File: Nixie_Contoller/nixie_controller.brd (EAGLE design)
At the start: 112.5 x 51.7 mm, 42 parts, among them IC1 DS1307, IC2 MAX1771ESA, IC3 7805T, J1 CON-SOCJ-2155, Q1 16MHz, T1 IRF644PBF, U1 328P, U2 HU2032-LF, X1 22-23-2021, Y2 32.768kHz

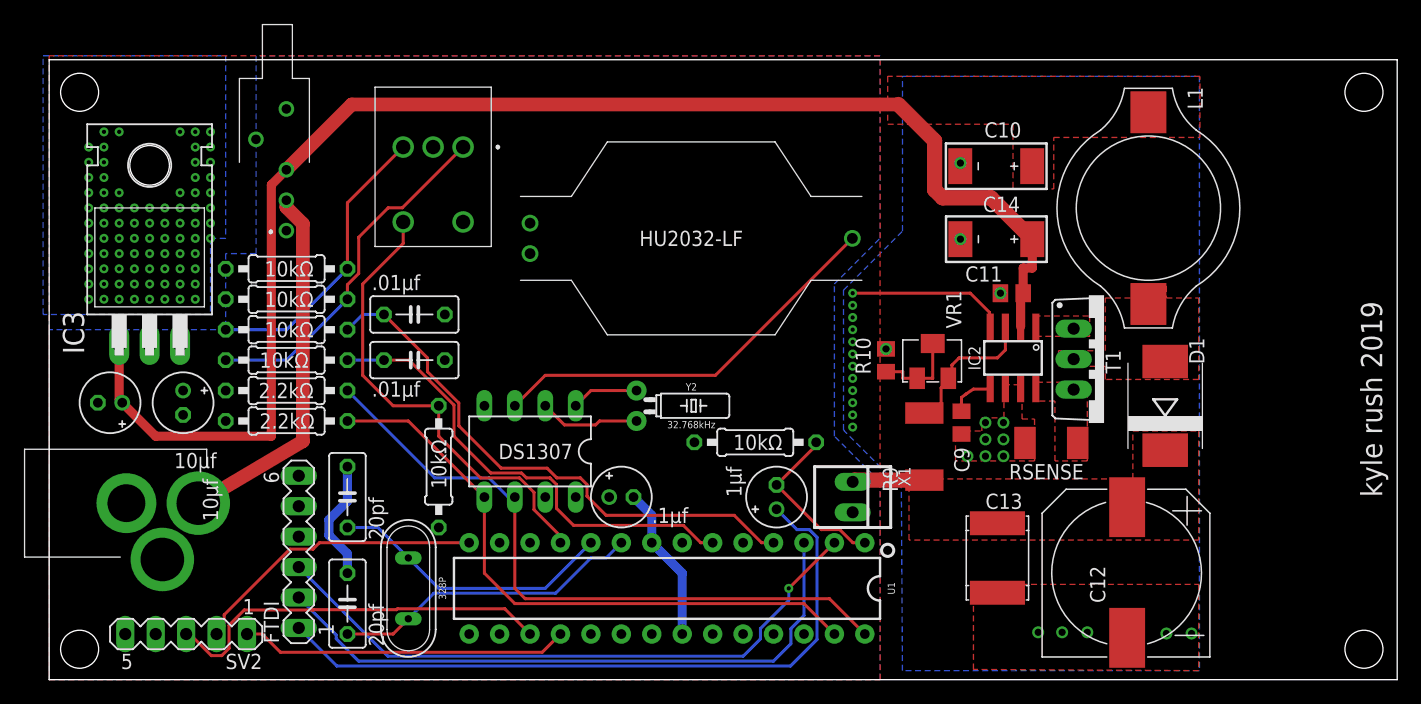
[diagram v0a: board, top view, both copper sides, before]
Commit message: Updates parts to Digikey equivalent, adds BOM, adds SHDN to pin 5
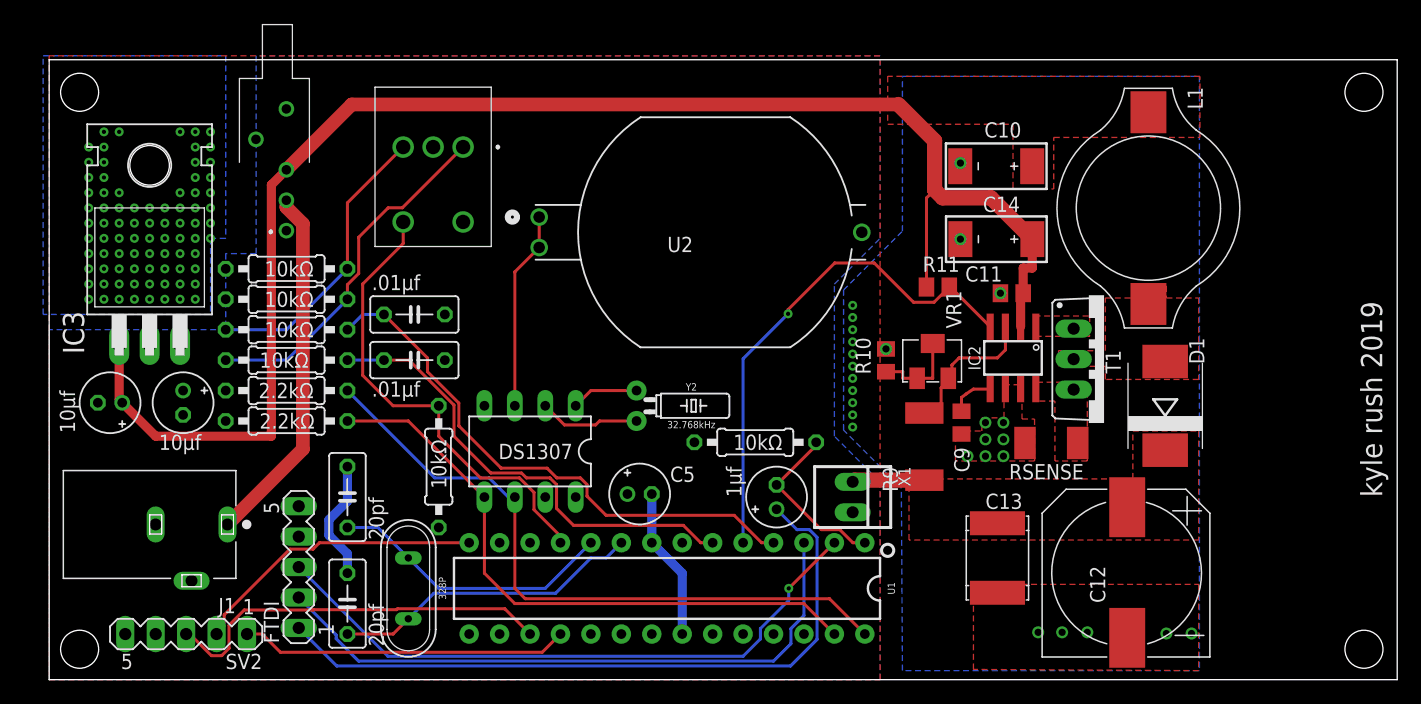
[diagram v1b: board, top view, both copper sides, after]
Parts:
- added R11: 10k, rcl:M0805
- C5: value .1μf -> .1uF
- FTDI: device con-lstb:MA06-1 -> con-lstb:MA05-1
- J1: value CON-SOCJ-2155 -> PJ-102A; device SamacSys_Parts:CONSOCJ2155 -> PJ-102A:CUI_PJ-102A
- U2: value HU2032-LF -> 120591-1; device SamacSys_Parts:HU2032LF -> TE Connectivity AMP Connectors 120591-1:CONN3_120591-1
- moved U2 14.2 mm to (54.4, 37.3)
- moved J1 4.44 mm to (8.38, 13.0), turned to 180 degrees
- moved C5 1.55 mm to (49.3, 15.5)
- moved FTDI 1.27 mm to (20.8, 9.40)
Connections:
- new net SHDN: IC2.4, R11.2, U1.5
- net +12V: now also R11.1
- net GND: now also FTDI.5; no longer FTDI.6, IC2.4, U2.1
- net N$1: now also U2.1
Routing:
- net SHDN: track 0.00 -> 42.7 mm, vias 0 -> 1
- net N$1: track 34.0 -> 16.6 mm
- net GND: track 36.6 -> 22.9 mm, vias 110 -> 109
- net +12V: track 121.1 -> 129.5 mm
- net N$6: track 30.8 -> 30.2 mm

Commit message: Production ready board with BOMS
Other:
- board text added: "kyle rush 2020"
- board text removed: "kyle rush 2019"
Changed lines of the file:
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@@
 <setting verticaltext="up"/>
 </settings>
-<grid distance="10" unitdist="mil" unit="mil" style="lines" multiple="1" display="no" altdistance="5" altunitdist="mil" altunit="mil"/>
+<grid distance="10" unitdist="mil" unit="mm" style="lines" multiple="1" display="no" altdistance="5" altunitdist="mil" altunit="mil"/>
 <layers>
 <layer number="1" name="Top" color="4" fill="1" visible="yes" active="yes"/>
@@
 <hole x="109.728" y="49.022" drill="3.175"/>
 <hole x="109.728" y="2.54" drill="3.175"/>
-<text x="111.252" y="15.24" size="1.778" layer="21" rot="R90">kyle rush 2019</text>
+<text x="111.252" y="15.24" size="1.778" layer="21" rot="R90">kyle rush 2020</text>
 <wire x1="-0.0254" y1="-63.5" x2="-0.0254" y2="-72.0852" width="0.2032" layer="47"/>
 <wire x1="-0.0254" y1="-72.0852" x2="-0.0254" y2="-73.66" width="0.2032" layer="47"/>
@@
 <element name="VR1" library="nick" package="BOURNS-3214W" value="5K" x="73.738" y="26.554" smashed="yes" rot="R270">
 <attribute name="NAME" x="74.858" y="32.472" size="1.27" layer="25" rot="R270"/>
-<attribute name="VALUE" x="74.36" y="31.146" size="1.27" layer="27" rot="R270"/>
 </element>
 <element name="C10" library="nick" package="C-EIA-7343" value="100uF,35V" x="79.038" y="42.854" smashed="yes" rot="R180">
@@
 </element>
 <element name="C11" library="rcl" package="C0805" value="100n" x="80.338" y="32.254" smashed="yes" rot="R180">
-<attribute name="NAME" x="76.449" y="33.224" size="1.27" layer="25"/>
+<attribute name="NAME" x="76.449" y="33.478" size="1.27" layer="25"/>
 <attribute name="VALUE" x="79.989" y="33.306" size="1.27" layer="27"/>
 </element>
@@
 <attribute name="POPULARITY" value="45" x="74.168" y="32.766" size="1.778" layer="27" display="off"/>
 <attribute name="SPICEPREFIX" value="R" x="74.168" y="32.766" size="1.778" layer="27" display="off"/>
-<attribute name="VALUE" x="72.898" y="30.226" size="1.27" layer="27"/>
 </element>
 <element name="FTDI" library="con-lstb" library_urn="urn:adsk.eagle:library:162" package="MA05-1" package3d_urn="urn:adsk.eagle:package:8332/1" value="" x="20.828" y="9.398" smashed="yes" rot="R90">

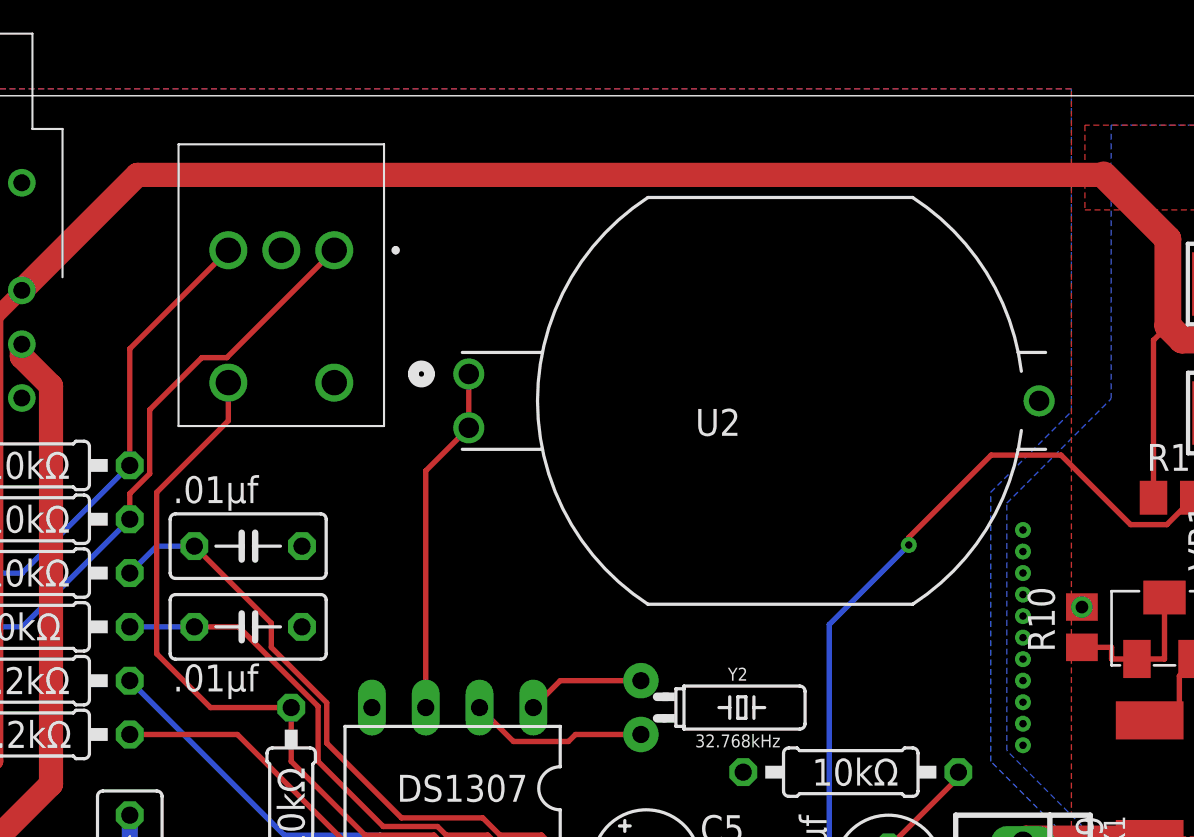
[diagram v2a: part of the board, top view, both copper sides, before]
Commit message: Reconfigures controller, configures clock to pull sketch down SHDN pin
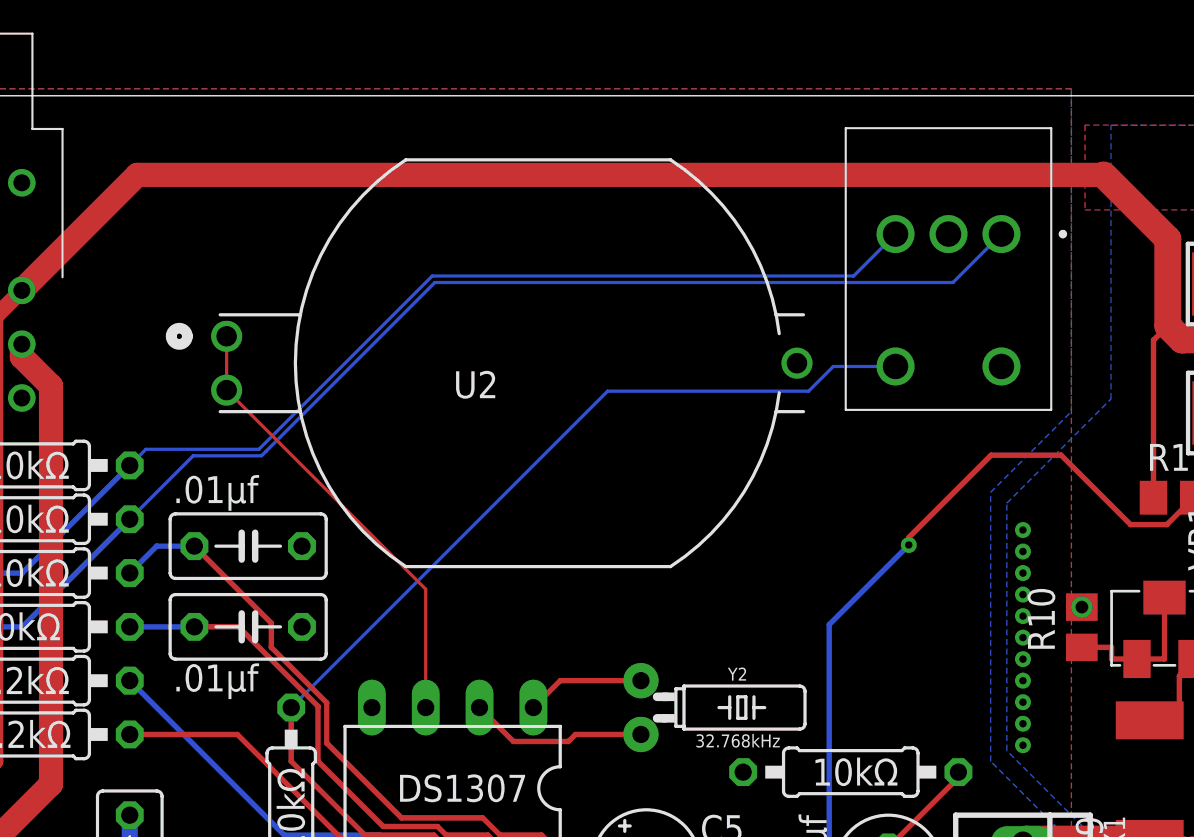
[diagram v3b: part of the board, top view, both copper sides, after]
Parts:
- moved VR2 31.5 mm to (66.0, 45.2)
- moved U2 11.6 mm to (42.9, 39.1)
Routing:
- net N$3: track 29.7 -> 59.0 mm
- net N$15: track 24.4 -> 52.9 mm
- net N$2: track 39.2 -> 52.7 mm
- net N$1: track 16.6 -> 21.4 mm
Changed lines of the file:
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@@
 <attribute name="MOUSER_PRICE-STOCK" value="https://www.mouser.com/Search/Refine.aspx?Keyword=633-A12AV" x="18.796" y="45.974" size="1.778" layer="27" rot="R180" display="off"/>
 </element>
-<element name="VR2" library="SamacSys_Parts" package="PEC092220FS0012" value="PEC09-2220F-S0012" x="34.544" y="44.45" smashed="yes" rot="R90">
-<attribute name="DESCRIPTION" value="Encoders 12PPR 24Detents 5V 2bit GrayCodeFlatted" x="34.544" y="44.45" size="1.778" layer="27" rot="R90" display="off"/>
-<attribute name="HEIGHT" value="11.35mm" x="34.544" y="44.45" size="1.778" layer="27" rot="R90" display="off"/>
-<attribute name="MANUFACTURER_NAME" value="Bourns" x="34.544" y="44.45" size="1.778" layer="27" rot="R90" display="off"/>
-<attribute name="MANUFACTURER_PART_NUMBER" value="PEC09-2220F-S0012" x="34.544" y="44.45" size="1.778" layer="27" rot="R90" display="off"/>
-<attribute name="MOUSER_PART_NUMBER" value="652-PEC092220FS0012" x="34.544" y="44.45" size="1.778" layer="27" rot="R90" display="off"/>
-<attribute name="MOUSER_PRICE-STOCK" value="https://www.mouser.com/Search/Refine.aspx?Keyword=652-PEC092220FS0012" x="34.544" y="44.45" size="1.778" layer="27" rot="R90" display="off"/>
+<element name="VR2" library="SamacSys_Parts" package="PEC092220FS0012" value="PEC09-2220F-S0012" x="66.04" y="45.212" smashed="yes" rot="R90">
+<attribute name="DESCRIPTION" value="Encoders 12PPR 24Detents 5V 2bit GrayCodeFlatted" x="66.04" y="45.212" size="1.778" layer="27" rot="R90" display="off"/>
+<attribute name="HEIGHT" value="11.35mm" x="66.04" y="45.212" size="1.778" layer="27" rot="R90" display="off"/>
+<attribute name="MANUFACTURER_NAME" value="Bourns" x="66.04" y="45.212" size="1.778" layer="27" rot="R90" display="off"/>
+<attribute name="MANUFACTURER_PART_NUMBER" value="PEC09-2220F-S0012" x="66.04" y="45.212" size="1.778" layer="27" rot="R90" display="off"/>
+<attribute name="MOUSER_PART_NUMBER" value="652-PEC092220FS0012" x="66.04" y="45.212" size="1.778" layer="27" rot="R90" display="off"/>
+<attribute name="MOUSER_PRICE-STOCK" value="https://www.mouser.com/Search/Refine.aspx?Keyword=652-PEC092220FS0012" x="66.04" y="45.212" size="1.778" layer="27" rot="R90" display="off"/>
 </element>
 <element name="IC3" library="linear" library_urn="urn:adsk.eagle:library:262" package="TO220H" package3d_urn="urn:adsk.eagle:package:16414/1" value="7805T" x="8.382" y="38.1" smashed="yes">
@@
 <attribute name="STANDARD" value="Manufacturer recommendations" x="8.382" y="12.954" size="1.778" layer="27" rot="R180" display="off"/>
 </element>
-<element name="U2" library="TE Connectivity AMP Connectors 120591-1" package="CONN3_120591-1" value="120591-1" x="54.356" y="37.338" smashed="yes">
-<attribute name="BUILT_BY" value="EMA_UL_Team" x="54.356" y="37.338" size="1.778" layer="27" display="off"/>
-<attribute name="COPYRIGHT" value="Copyright (C) 2016 Accelerated Designs. All rights reserved" x="54.356" y="37.338" size="1.778" layer="27" display="off"/>
-<attribute name="DESCRIPTION" value="TOP LOAD BATTERY" x="54.356" y="37.338" size="1.778" layer="27" display="off"/>
-<attribute name="MANUFACTURER_PART_NUMBER" value="120591-1" x="54.356" y="37.338" size="1.778" layer="27" display="off"/>
-<attribute name="NAME" x="51.5874" y="35.687" size="1.27" layer="25" ratio="6" rot="SR0"/>
-<attribute name="PITCH_MM_" value="-" x="54.356" y="37.338" size="1.778" layer="27" display="off"/>
-<attribute name="POSITIONS" value="2" x="54.356" y="37.338" size="1.778" layer="27" display="off"/>
-<attribute name="PRODUCT" value="Battery Holders" x="54.356" y="37.338" size="1.778" layer="27" display="off"/>
-<attribute name="ROWS-CONFIG" value="-" x="54.356" y="37.338" size="1.778" layer="27" display="off"/>
-<attribute name="TE_PART_NUMBER" value="120591-1" x="54.356" y="37.338" size="1.778" layer="27" display="off"/>
-<attribute name="TYPE" value="Coin Cell" x="54.356" y="37.338" size="1.778" layer="27" display="off"/>
-<attribute name="VENDOR" value="TE Connectivity" x="54.356" y="37.338" size="1.778" layer="27" display="off"/>
+<element name="U2" library="TE Connectivity AMP Connectors 120591-1" package="CONN3_120591-1" value="120591-1" x="42.926" y="39.116" smashed="yes">
+<attribute name="BUILT_BY" value="EMA_UL_Team" x="42.926" y="39.116" size="1.778" layer="27" display="off"/>
+<attribute name="COPYRIGHT" value="Copyright (C) 2016 Accelerated Designs. All rights reserved" x="42.926" y="39.116" size="1.778" layer="27" display="off"/>
+<attribute name="DESCRIPTION" value="TOP LOAD BATTERY" x="42.926" y="39.116" size="1.778" layer="27" display="off"/>
+<attribute name="MANUFACTURER_PART_NUMBER" value="120591-1" x="42.926" y="39.116" size="1.778" layer="27" display="off"/>
+<attribute name="NAME" x="40.1574" y="37.465" size="1.27" layer="25" ratio="6" rot="SR0"/>
+<attribute name="PITCH_MM_" value="-" x="42.926" y="39.116" size="1.778" layer="27" display="off"/>
+<attribute name="POSITIONS" value="2" x="42.926" y="39.116" size="1.778" layer="27" display="off"/>
+<attribute name="PRODUCT" value="Battery Holders" x="42.926" y="39.116" size="1.778" layer="27" display="off"/>
+<attribute name="ROWS-CONFIG" value="-" x="42.926" y="39.116" size="1.778" layer="27" display="off"/>
+<attribute name="TE_PART_NUMBER" value="120591-1" x="42.926" y="39.116" size="1.778" layer="27" display="off"/>
+<attribute name="TYPE" value="Coin Cell" x="42.926" y="39.116" size="1.778" layer="27" display="off"/>
+<attribute name="VENDOR" value="TE Connectivity" x="42.926" y="39.116" size="1.778" layer="27" display="off"/>
 </element>
 </elements>
@@
 <contactref element="U2" pad="3"/>
 <contactref element="U2" pad="1"/>
-<wire x1="38.862" y1="22.86" x2="38.862" y2="34.036" width="0.254" layer="1"/>
-<wire x1="38.862" y1="34.036" x2="40.894" y2="36.068" width="0.254" layer="1"/>
-<wire x1="40.894" y1="38.608" x2="40.894" y2="36.068" width="0.254" layer="1"/>
+<wire x1="29.464" y1="40.386" x2="29.464" y2="37.846" width="0.1524" layer="1"/>
+<wire x1="29.464" y1="37.846" x2="38.862" y2="28.448" width="0.1524" layer="1"/>
+<wire x1="38.862" y1="28.448" x2="38.862" y2="22.86" width="0.1524" layer="1"/>
 </signal>
 <signal name="GND" class="1">
@@
 <contactref element="R4" pad="1"/>
 <contactref element="VR2" pad="A1"/>
-<wire x1="29.4734" y1="39.3794" x2="28.293475" y2="39.3794" width="0.254" layer="1"/>
-<wire x1="24.892" y1="32.96091875" x2="24.892" y2="31.75" width="0.254" layer="1"/>
-<wire x1="25.8318" y1="33.90071875" x2="24.892" y2="32.96091875" width="0.254" layer="1"/>
-<wire x1="28.293475" y1="39.3794" x2="25.8318" y2="36.917725" width="0.254" layer="1"/>
-<wire x1="25.8318" y1="36.917725" x2="25.8318" y2="33.90071875" width="0.254" layer="1"/>
-<wire x1="34.544" y1="44.45" x2="29.4734" y2="39.3794" width="0.254" layer="1"/>
 <wire x1="24.892" y1="31.75" x2="19.812" y2="26.67" width="0.254" layer="16"/>
 <wire x1="19.812" y1="26.67" x2="14.732" y2="26.67" width="0.254" layer="16"/>
+<wire x1="24.892" y1="31.75" x2="27.8892" y2="34.7472" width="0.1524" layer="16"/>
+<wire x1="27.8892" y1="34.7472" x2="31.11425625" y2="34.7472" width="0.1524" layer="16"/>
+<wire x1="31.11425625" y1="34.7472" x2="31.330528125" y2="34.963471875" width="0.1524" layer="16"/>
+<wire x1="31.330528125" y1="34.963471875" x2="39.29305625" y2="42.926" width="0.1524" layer="16"/>
+<wire x1="63.754" y1="42.926" x2="66.04" y2="45.212" width="0.1524" layer="16"/>
+<wire x1="39.29305625" y1="42.926" x2="63.754" y2="42.926" width="0.1524" layer="16"/>
 </signal>
 <signal name="N$15">
@@
 <contactref element="R3" pad="1"/>
 <contactref element="VR2" pad="B1"/>
-<wire x1="29.544" y1="44.45" x2="24.892" y2="39.798" width="0.254" layer="1"/>
-<wire x1="24.892" y1="39.798" x2="24.892" y2="34.29" width="0.254" layer="1"/>
 <wire x1="24.892" y1="34.29" x2="19.812" y2="29.21" width="0.254" layer="16"/>
 <wire x1="19.812" y1="29.21" x2="14.732" y2="29.21" width="0.254" layer="16"/>
+<wire x1="24.892" y1="34.29" x2="25.654" y2="35.052" width="0.1524" layer="16"/>
+<wire x1="30.988" y1="35.052" x2="25.654" y2="35.052" width="0.1524" layer="16"/>
+<wire x1="61.04" y1="45.212" x2="59.0588" y2="43.2308" width="0.1524" layer="16"/>
+<wire x1="59.0588" y1="43.2308" x2="39.1668" y2="43.2308" width="0.1524" layer="16"/>
+<wire x1="39.1668" y1="43.2308" x2="30.988" y2="35.052" width="0.1524" layer="16"/>
 </signal>
 <signal name="N$9">
@@
 <wire x1="39.25128125" y1="16.8402" x2="40.4622" y2="15.62928125" width="0.254" layer="1"/>
 <wire x1="40.4622" y1="15.62928125" x2="40.4622" y2="14.19031875" width="0.254" layer="1"/>
-<wire x1="29.544" y1="38.2" x2="29.544" y2="36.402" width="0.254" layer="1"/>
-<wire x1="26.162" y1="25.4" x2="28.702" y2="22.86" width="0.254" layer="1"/>
-<wire x1="28.702" y1="22.86" x2="32.512" y2="22.86" width="0.254" layer="1"/>
-<wire x1="29.544" y1="36.402" x2="26.162" y2="33.02" width="0.254" layer="1"/>
-<wire x1="26.162" y1="33.02" x2="26.162" y2="25.4" width="0.254" layer="1"/>
 <wire x1="32.512" y1="22.86" x2="32.512" y2="20.32" width="0.254" layer="1"/>
 <wire x1="39.25128125" y1="16.8402" x2="35.9918" y2="16.8402" width="0.254" layer="1"/>
 <wire x1="35.9918" y1="16.8402" x2="32.512" y2="20.32" width="0.254" layer="1"/>
+<wire x1="58.10189375" y1="38.962" x2="61.04" y2="38.962" width="0.1524" layer="16"/>
+<wire x1="56.93509375" y1="37.7952" x2="58.10189375" y2="38.962" width="0.1524" layer="16"/>
+<wire x1="32.512" y1="22.86" x2="47.4472" y2="37.7952" width="0.1524" layer="16"/>
+<wire x1="47.4472" y1="37.7952" x2="56.93509375" y2="37.7952" width="0.1524" layer="16"/>
 </signal>
 <signal name="N$14">
